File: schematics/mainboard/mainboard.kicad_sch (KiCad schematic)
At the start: 32 parts, among them J1 ICSP, J2 USB_B_Micro, J3 DEALON DC-S050-200, J4 PWR_SELECT, J5 JOY1, J6 JOY2, J7 Throttle, J8 DGAUGES, U1 ATmega2560-16A, U2 FT232RL, U3 USBLC6-2P6, U4 AIP78M05, U5 L9110, Y1 16Mhz

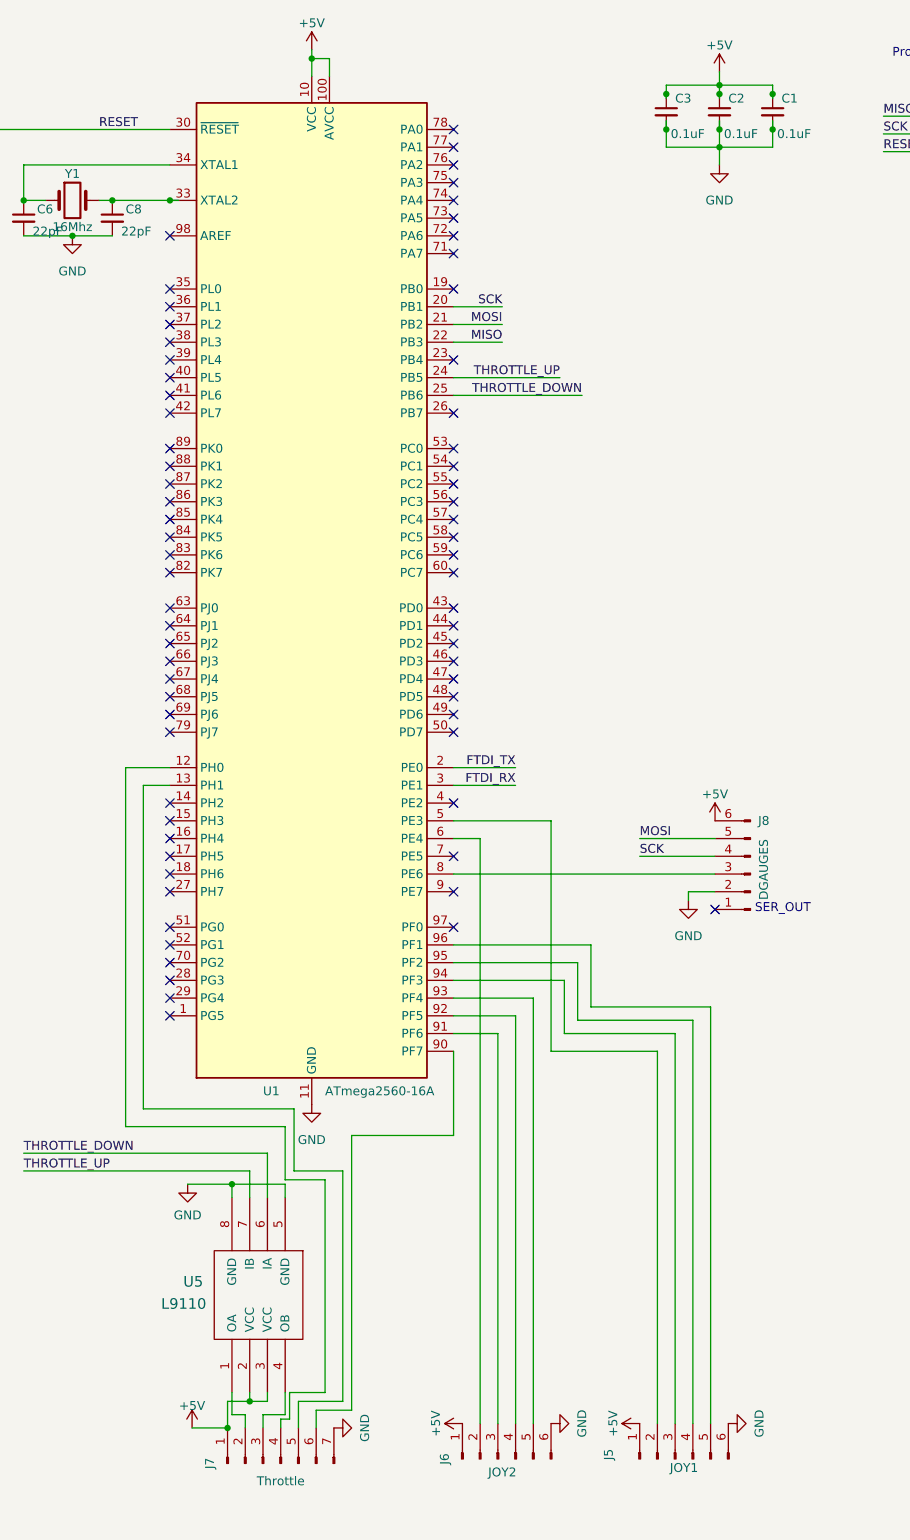
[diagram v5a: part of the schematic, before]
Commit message: Mainboard: tweak pins, routed lcd connector
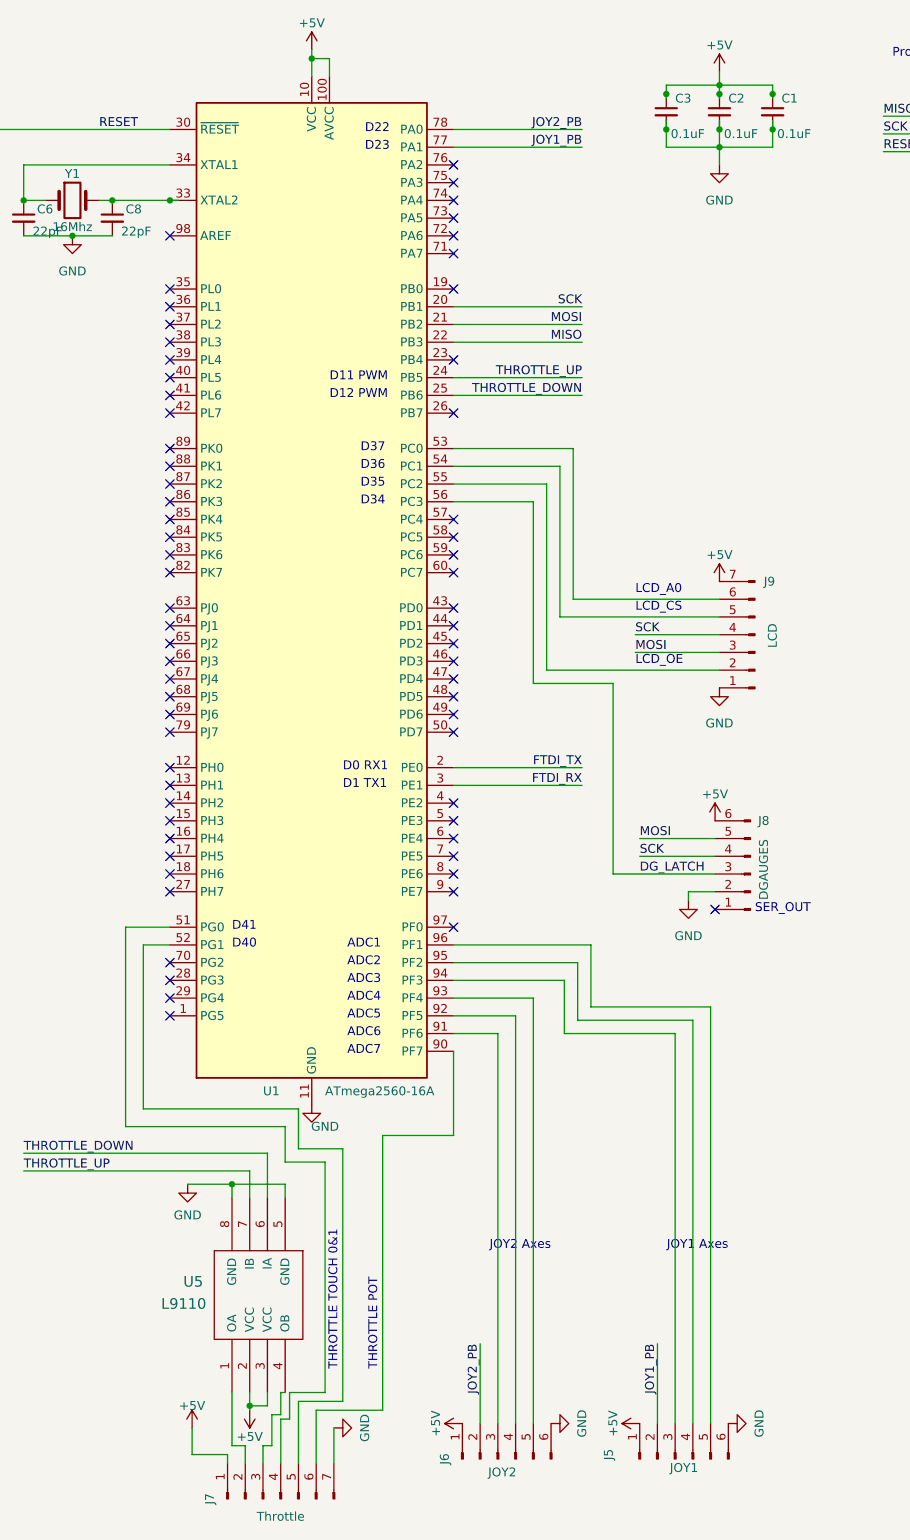
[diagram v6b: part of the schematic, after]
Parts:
- added J9: LCD, Connector_JST:JST_PH_B7B-PH-K_1x07_P2.00mm_Vertical, symbol Connector:Conn_01x07_Pin
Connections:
- net +5V: now also J9.7 (Pin_7)
- net GND: now also J9.1 (Pin_1)
- net MOSI: now also J9.3 (Pin_3)
- net SCK: now also J9.4 (Pin_4)
- net at U1.12 (PH0): no longer J7.4 (Pin_4)
- net at U1.13 (PH1): no longer J7.5 (Pin_5)
- net at U1.5 (PE3): no longer J5.2 (Pin_2)
- net at U1.51 (PG0): now also J7.4 (Pin_4)
- net at U1.52 (PG1): now also J7.5 (Pin_5)
- net at U1.53 (PC0): now also J9.6 (Pin_6)
- net at U1.54 (PC1): now also J9.5 (Pin_5)
- net at U1.55 (PC2): now also J9.2 (Pin_2)
- net DG_LATCH: now reaches U1.56 (PC3)
- net DG_LATCH: now also J8.3 (Pin_3)
- net at U1.6 (PE4): no longer J6.2 (Pin_2)
- net JOY1_PB: now reaches U1.77 (PA1)
- net JOY1_PB: now also J5.2 (Pin_2)
- net JOY2_PB: now reaches U1.78 (PA0)
- net JOY2_PB: now also J6.2 (Pin_2)
- net at U1.8 (PE6): no longer J8.3 (Pin_3)
- no-connect marks 83 -> 80
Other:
- note added: "ADC1"
- note added: "ADC2"
- note added: "ADC3"
- note added: "ADC4"
- note added: "ADC5"
- note added: "ADC6"
- note added: "ADC7"
- note added: "D0 RX1"
- note added: "D1 TX1"
- note added: "D11 PWM"
- note added: "D12 PWM"
- note added: "D22"
- note added: "D23"
- note added: "D34"
- note added: "D35"
- note added: "D36"
- note added: "D37"
- note added: "D40"
- note added: "D41"
- note added: "JOY1 Axes"
- note added: "JOY2 Axes"
- note added: "LCD_A0"
- note added: "LCD_CS"
- note added: "LCD_OE"
- note added: "THROTTLE POT"
- note added: "THROTTLE TOUCH 0&1"
- moved on the sheet: J7

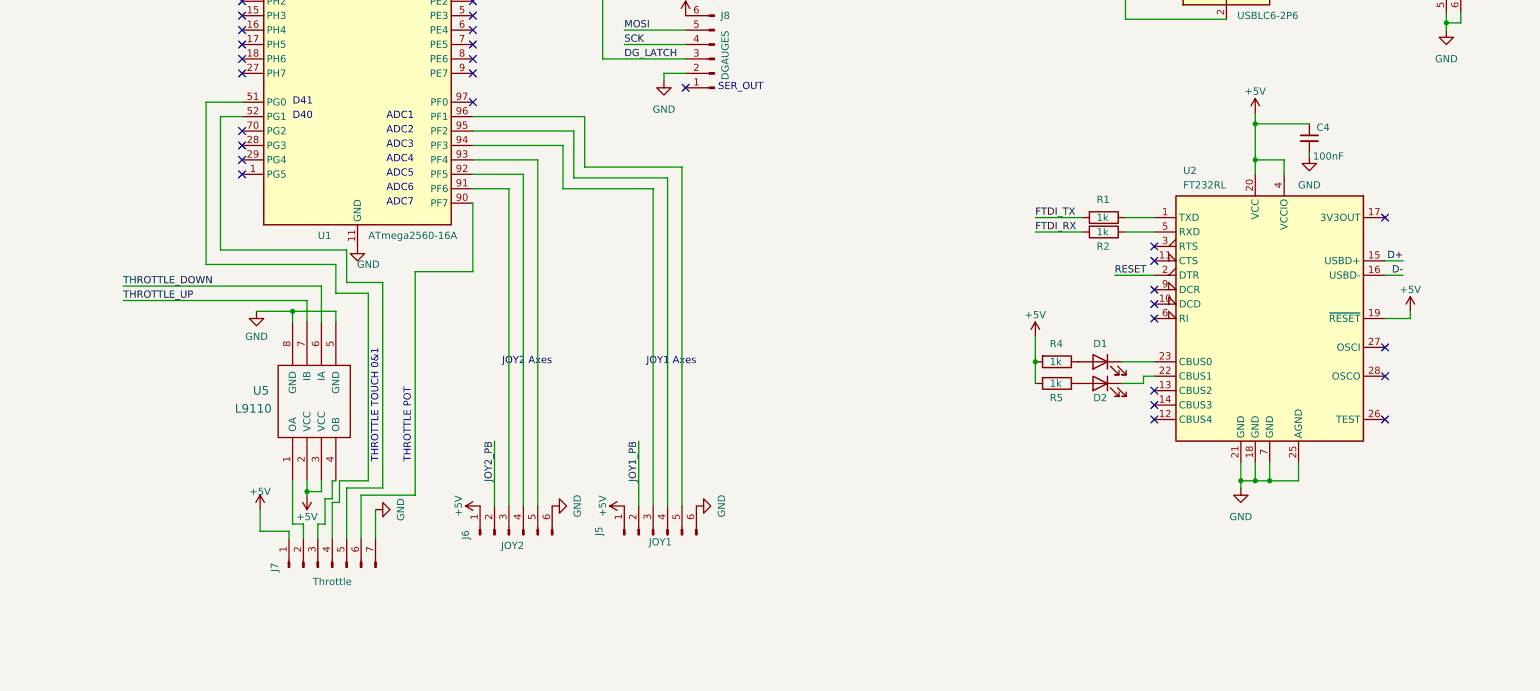
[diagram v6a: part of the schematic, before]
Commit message: SCH: mainboard missing cap & gnd connections on ft232
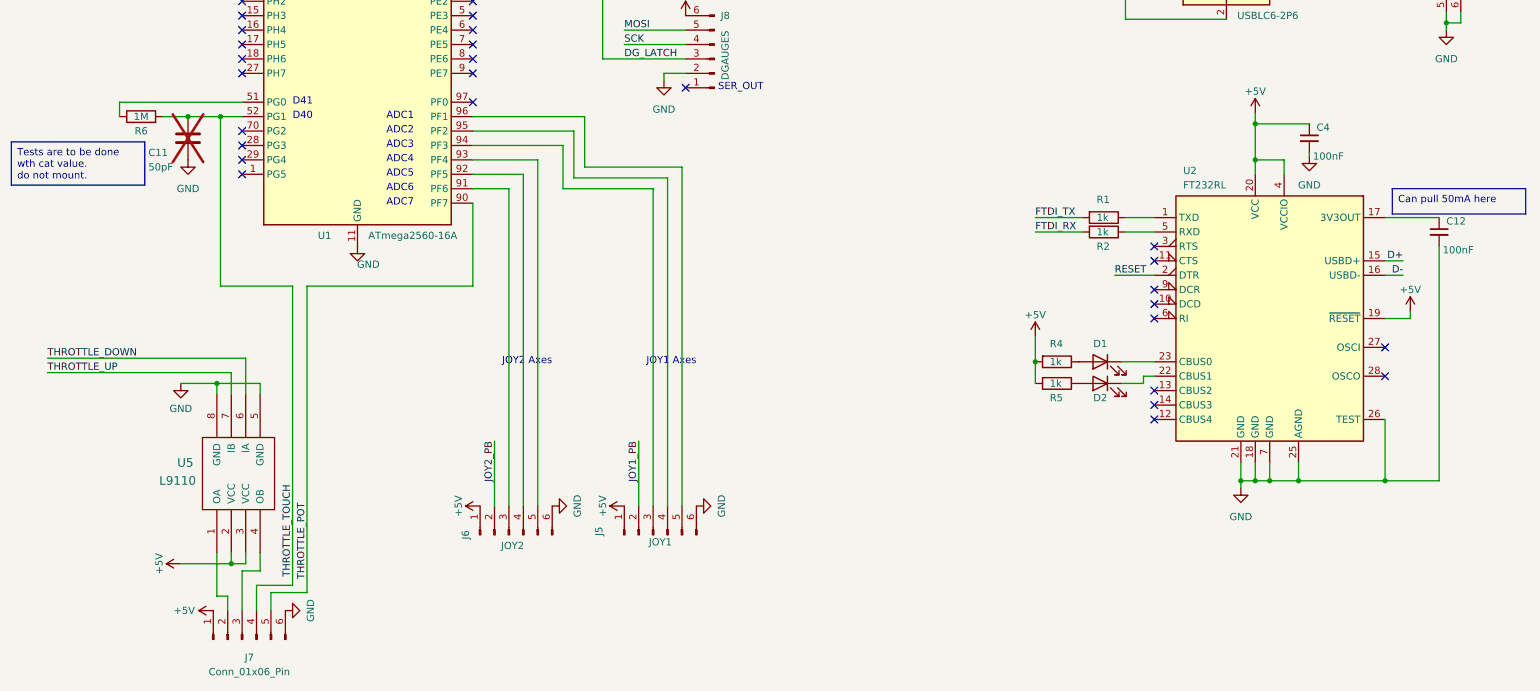
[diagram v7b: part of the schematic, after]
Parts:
- removed J7: Throttle, Connector_JST:JST_PH_B7B-PH-K_1x07_P2.00mm_Vertical, symbol Connector:Conn_01x07_Pin
- added C11: 50pF, Capacitor_SMD:C_0603_1608Metric, symbol Device:C
- added C12: 100nF, Capacitor_SMD:C_0603_1608Metric, symbol Device:C_Small
- added J7: Conn_01x06_Pin, Connector_JST:JST_PH_B6B-PH-K_1x06_P2.00mm_Vertical, symbol Connector:Conn_01x06_Pin
- added R6: 1M, Resistor_SMD:R_0603_1608Metric, symbol Device:R
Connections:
- net +5V: now also J7.1 (Pin_1)
- net GND: now also U2.26 (TEST), C11.2, C12.2, J7.6 (Pin_6)
- net at U5.1 (OA): now also J7.2 (Pin_2)
- net at U5.4 (OB): now also J7.3 (Pin_3)
- net at U1.51 (PG0): now also R6.1
- net THROTTLE_TOUCH: now reaches U1.52 (PG1)
- net THROTTLE_TOUCH: now also C11.1, J7.4 (Pin_4), R6.2
- net THROTTLE_POT: now reaches U1.90 (PF7)
- net THROTTLE_POT: now also J7.5 (Pin_5)
- net at U2.17 (3V3OUT): now also C12.1
- no-connect marks 80 -> 78
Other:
- note removed: "THROTTLE POT"
- note removed: "THROTTLE TOUCH 0&1"
- moved on the sheet: U5

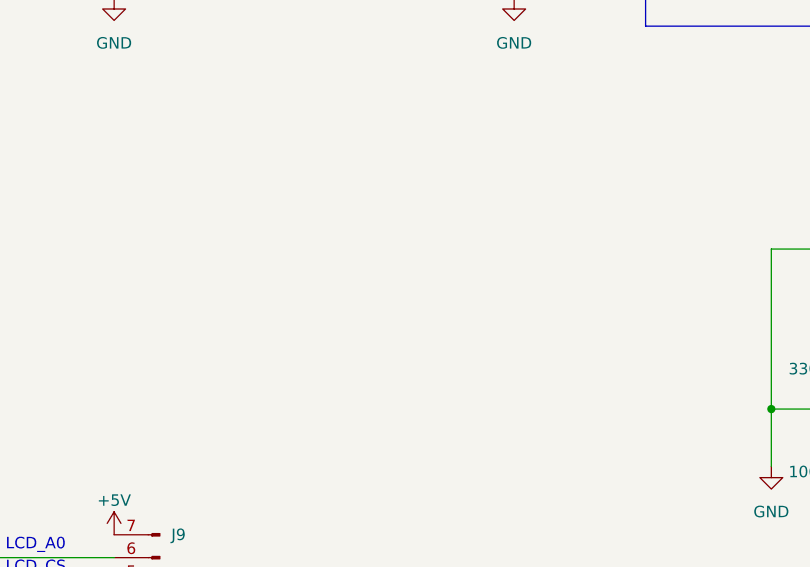
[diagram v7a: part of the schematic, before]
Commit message: SCH: Mainboard: add power LED
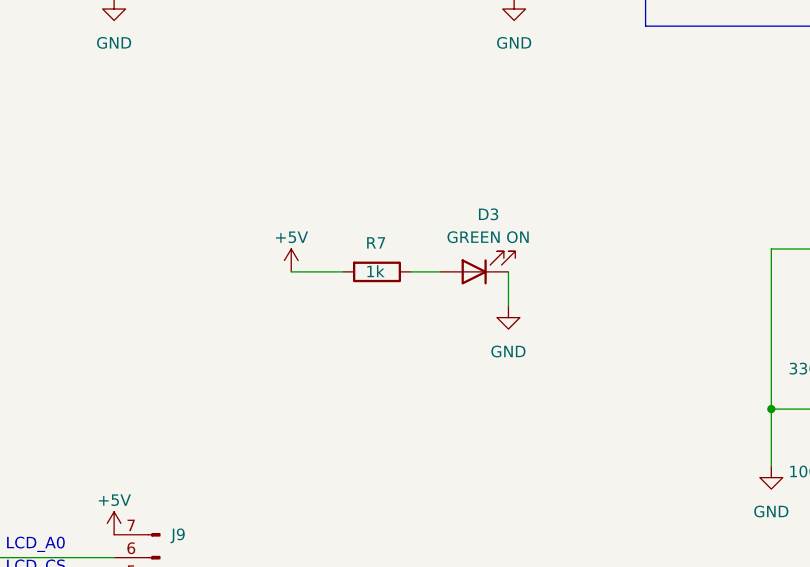
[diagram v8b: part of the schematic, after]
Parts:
- added D3: GREEN ON, LED_SMD:LED_0603_1608Metric, symbol Device:LED
- added R7: 1k, Resistor_SMD:R_0603_1608Metric, symbol Device:R
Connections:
- net +5V: now also R7.2
- net GND: now also D3.1 (K)
- new net: D3.2 (A), R7.1
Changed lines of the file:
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@@
+    (stroke (width 0) (type default))
+  )
+  (wire (pts (xy 286.385 143.51) (xy 289.56 143.51))
     (stroke (width 0) (type default))
   )
@@
     (stroke (width 0) (type default))
   )
+  (wire (pts (xy 273.05 143.51) (xy 278.765 143.51))
+    (stroke (width 0) (type default))
+  )
   (wire (pts (xy 347.98 179.07) (xy 347.98 187.325))
     (stroke (width 0) (type default))
@@
   )
   (wire (pts (xy 226.695 187.325) (xy 238.125 187.325))
+    (stroke (width 0) (type default))
+  )
+  (wire (pts (xy 297.18 143.51) (xy 297.18 147.32))
     (stroke (width 0) (type default))
   )
@@
     )
   )
+  (symbol (lib_id "power:+5V") (at 273.05 143.51 0) (unit 1)
+    (in_bom yes) (on_board yes) (dnp no) (fields_autoplaced)
+    (property "Reference" "#PWR034" (at 273.05 147.32 0)
+      (effects (font (size 1.27 1.27)) hide)
+    )
+    (property "Value" "+5V" (at 273.05 139.7 0)
+      (effects (font (size 1.27 1.27)))
+    )
+    (property "Footprint" "" (at 273.05 143.51 0)
+      (effects (font (size 1.27 1.27)) hide)
+    )
+    (property "Datasheet" "" (at 273.05 143.51 0)
+      (effects (font (size 1.27 1.27)) hide)
+    )
+    (pin "1")
+    (instances
+      (project "mainboard"
+        (path "/d7de281c-a164-4408-aff7-47d87383fb97"
+          (reference "#PWR034") (unit 1)
+        )
+      )
+    )
+  )
   (symbol (lib_id "power:GND") (at 144.145 119.38 0) (unit 1)
     (in_bom yes) (on_board yes) (dnp no) (fields_autoplaced)
@@
         (path "/d7de281c-a164-4408-aff7-47d87383fb97"
           (reference "J7") (unit 1)
+        )
+      )
+    )
+  )
+  (symbol (lib_id "Device:LED") (at 293.37 143.51 180) (unit 1)
+    (in_bom yes) (on_board yes) (dnp no) (fields_autoplaced)
+    (property "Reference" "D3" (at 294.9575 137.16 0)
+      (effects (font (size 1.27 1.27)))
+    )
+    (property "Value" "GREEN ON" (at 294.9575 139.7 0)
+      (effects (font (size 1.27 1.27)))
+    )
+    (property "Footprint" "LED_SMD:LED_0603_1608Metric" (at 293.37 143.51 0)
+      (effects (font (size 1.27 1.27)) hide)
+    )
+    (property "Datasheet" "~" (at 293.37 143.51 0)
+      (effects (font (size 1.27 1.27)) hide)
+    )
+    (pin "1")
+    (pin "2")
+    (instances
+      (project "mainboard"
+        (path "/d7de281c-a164-4408-aff7-47d87383fb97"
+          (reference "D3") (unit 1)
         )
       )
@@
     )
   )
+  (symbol (lib_id "Device:R") (at 282.575 143.51 270) (unit 1)
+    (in_bom yes) (on_board yes) (dnp no)
+    (property "Reference" "R7" (at 281.305 140.335 90)
+      (effects (font (size 1.27 1.27)) (justify left))
+    )
+    (property "Value" "1k" (at 281.305 143.51 90)
+      (effects (font (size 1.27 1.27)) (justify left))
+    )
+    (property "Footprint" "Resistor_SMD:R_0603_1608Metric" (at 282.575 141.732 90)
+      (effects (font (size 1.27 1.27)) hide)
+    )
+    (property "Datasheet" "~" (at 282.575 143.51 0)
+      (effects (font (size 1.27 1.27)) hide)
+    )
+    (property "lcsc" "C21190" (at 282.575 143.51 90)
+      (effects (font (size 1.27 1.27)) hide)
+    )
+    (pin "1")
+    (pin "2")
+    (instances
+      (project "mainboard"
+        (path "/d7de281c-a164-4408-aff7-47d87383fb97"
+          (reference "R7") (unit 1)
+        )
+      )
+    )
+  )
   (symbol (lib_id "Device:R") (at 156.845 224.79 90) (unit 1)
     (in_bom yes) (on_board yes) (dnp no)
@@
         )
       )
+    )
+  )
+  (symbol (lib_id "power:GND") (at 297.18 147.32 0) (unit 1)
+    (in_bom yes) (on_board yes) (dnp no) (fields_autoplaced)
+    (property "Reference" "#PWR035" (at 297.18 153.67 0)
+      (effects (font (size 1.27 1.27)) hide)
+    )
+    (property "Value" "GND" (at 297.18 152.4 0)
+      (effects (font (size 1.27 1.27)))
+    )
+    (property "Footprint" "" (at 297.18 147.32 0)
+      (effects (font (size 1.27 1.27)) hide)
+    )
+    (property "Datasheet" "" (at 297.18 147.32 0)
+      (effects (font (size 1.27 1.27)) hide)
+    )
+    (pin "1")
+    (instances
+      (project "mainboard"
+        (path "/d7de281c-a164-4408-aff7-47d87383fb97"
+          (reference "#PWR035") (unit 1)
+        )
+      )
